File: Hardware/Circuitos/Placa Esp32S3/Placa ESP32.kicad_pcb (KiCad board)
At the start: 2 copper layers, 50 x 50 mm, 9 parts, among them J1 Conn_01x04, J3 ESP32-S3-Touch-LCD-3.5B, J4 Conn_01x02, J8 Conn_01x02

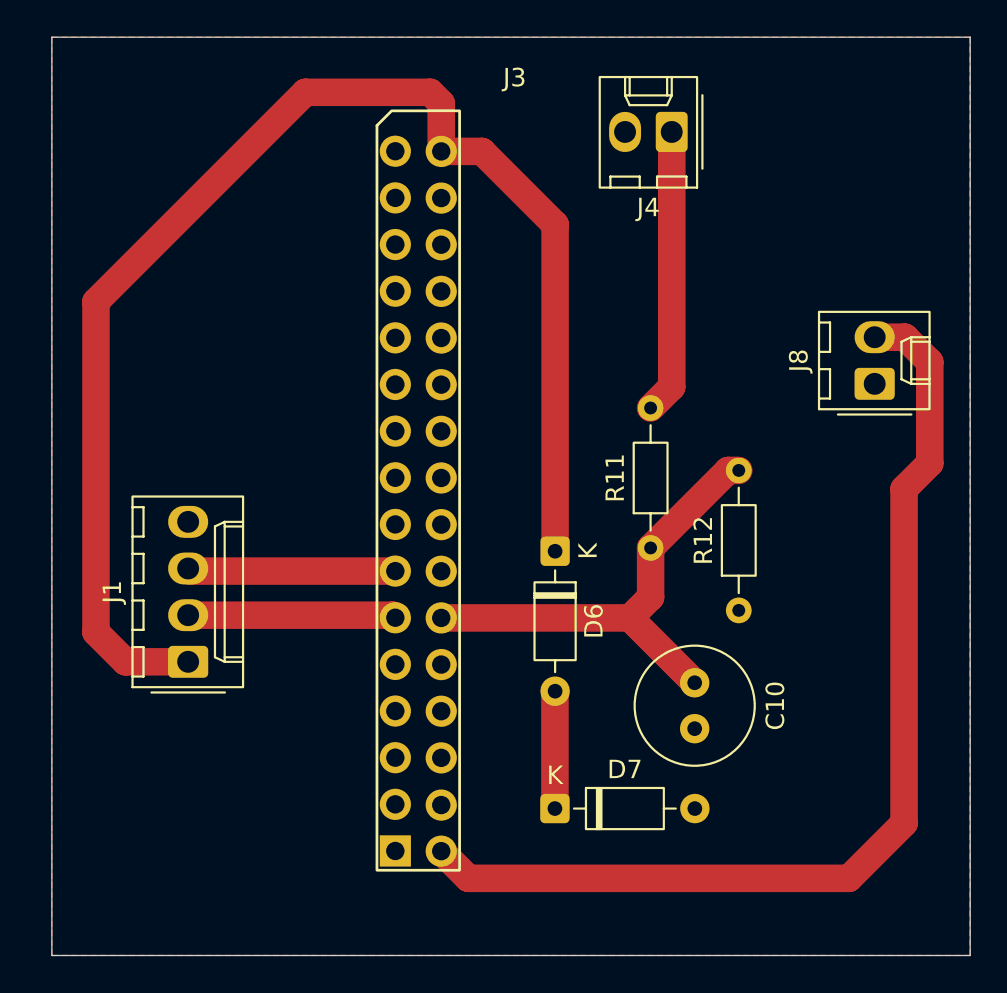
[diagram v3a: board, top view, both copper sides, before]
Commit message: Placa ESP32 - Colocar componentes en la PCB
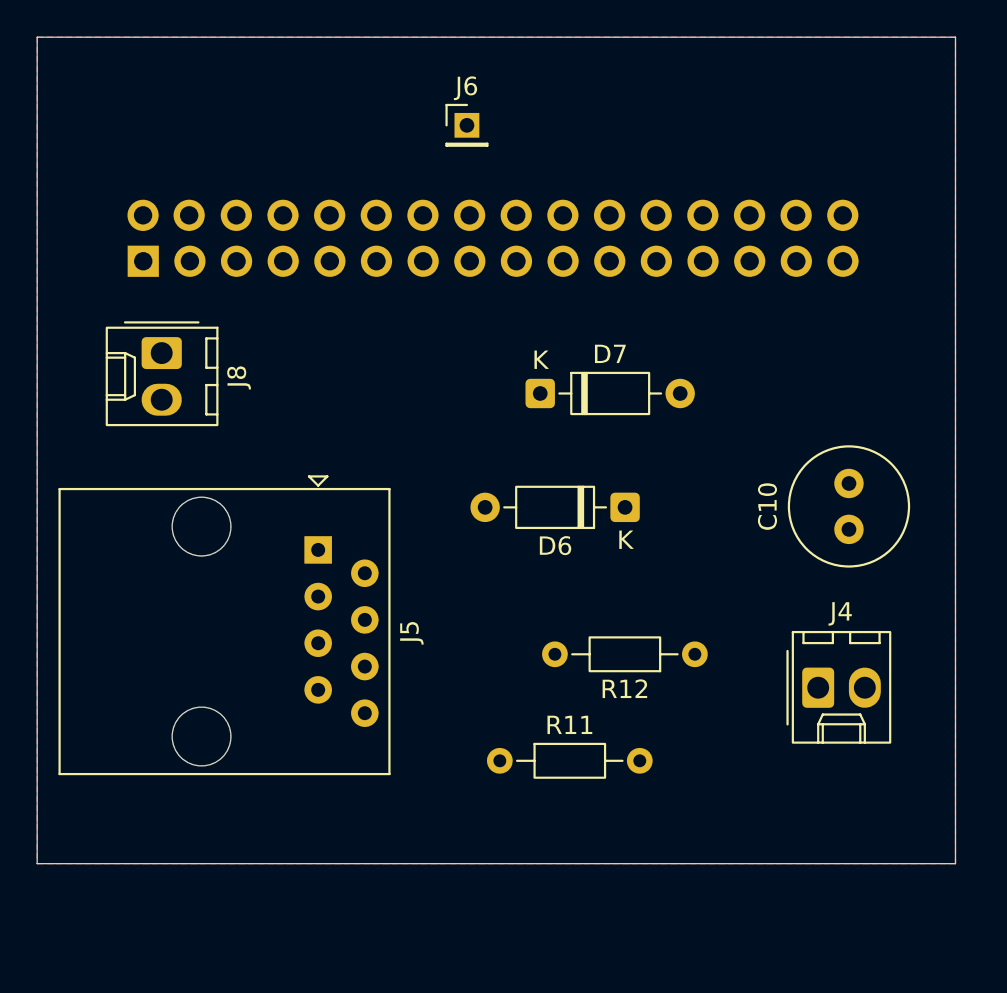
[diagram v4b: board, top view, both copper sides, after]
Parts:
- removed J1: Conn_01x04, Connector_Molex:Molex_KK-254_AE-6410-04A_1x04_P2.54mm_Vertical
- added J5: Conn_01x08, Connector_RJ:RJ45_Amphenol_54602-x08_Horizontal, F.Cu at (84.1, 103.3)
- added J6: Conn_01x01, Connector_PinHeader_2.00mm:PinHeader_1x01_P2.00mm_Vertical, F.Cu at (92.2, 80.2)
- J3: moved to B.Cu
- moved J8 38.9 mm to (75.6, 92.6), turned to -90 degrees
- moved J4 31.3 mm to (111.3, 110.8), turned to 0 degrees
- moved D7 22.6 mm to (96.2, 94.8)
- moved J3 19.6 mm to (93.6, 81.1), turned to 90 degrees
- moved R11 14.2 mm to (94.0, 114.8), turned to 0 degrees
- moved C10 11.8 mm to (113.0, 102.2), turned to 90 degrees
- moved D6 4.50 mm to (100.8, 101.0), turned to 180 degrees
- moved R12 3.38 mm to (104.6, 109.0), turned to 180 degrees
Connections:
- J3 pad 10: /GPIO11 (MQ-2) -> unconnected-(J3-GPIO11-Pad10)
- J3 pad 11: /GPIO40 -> unconnected-(J3-GPIO40-Pad11)
- J3 pad 12: /GPIO10 (Entrada Murata) -> unconnected-(J3-GPIO10-Pad12)
- J3 pad 13: /GPIO41 -> unconnected-(J3-GPIO41-Pad13)
- J3 pad 16: unconnected-(J3-GPIO17-Pad16) -> /GPIO17 (MQ-9)
- J3 pad 18: unconnected-(J3-GPIO18-Pad18) -> /GPIO18 (Entrada Murata)
- J3 pad 7: unconnected-(J3-GPIO38-Pad7) -> /GPIO38 D
- J3 pad 9: unconnected-(J3-GPIO39-Pad9) -> /GPIO39 C
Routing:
- net /3.3V: track 75.7 -> 0.00 mm
- net /5V: track 56.3 -> 0.00 mm
- net /GPIO10 (Entrada Murata): track 26.1 -> 0.00 mm
- net Net-(J4-Pin_1): track 15.5 -> 0.00 mm
- net /GPIO41: track 11.3 -> 0.00 mm
- net /GPIO40: track 11.3 -> 0.00 mm
- net Net-(D6-A): track 6.39 -> 0.00 mm
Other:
- board size 50 x 50 mm -> 50 x 45 mm

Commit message: Placa ESP32 - Rutear componentes
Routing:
- net /3.3V: track 0.00 -> 46.5 mm
- net /GPIO10 (Entrada Murata): track 0.00 -> 25.9 mm
- net /GPIO38 D: track 0.00 -> 20.9 mm
- net /GPIO39 C: track 0.00 -> 17.8 mm
- net /5V: track 0.00 -> 15.6 mm
- net Net-(J4-Pin_1): track 0.00 -> 11.4 mm
- net Net-(D6-A): track 0.00 -> 7.44 mm
- net /GPIO17 (MQ-9): track 0.00 -> 4.96 mm

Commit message: Placa ESP32 - Corrección de pista
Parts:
- moved J6 5.41 mm to (86.8, 79.8)
- moved J3 1.60 mm to (92.0, 81.1)
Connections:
- C10 pad 1: /GPIO10 (Entrada Murata) -> /GPIO18 (Entrada Murata)
- R11 pad 1: /GPIO10 (Entrada Murata) -> /GPIO18 (Entrada Murata)
- R12 pad 2: /GPIO10 (Entrada Murata) -> /GPIO18 (Entrada Murata)
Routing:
- net /GPIO18 (Entrada Murata): track 0.00 -> 75.1 mm
- net /GPIO10 (Entrada Murata): track 25.9 -> 0.00 mm
- net /GPIO17 (MQ-9): track 4.96 -> 8.34 mm
- net /3.3V: track 46.5 -> 45.7 mm
